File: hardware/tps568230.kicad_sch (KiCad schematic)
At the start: 30 parts, among them U3 TPS568230, U4 LD39050PU33R

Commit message: Annotating components
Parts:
- renumbered TP1 to TP2, TP2 to TP4
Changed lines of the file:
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@@
 		(dnp no)
 		(fields_autoplaced yes)
-		(property "Reference" "#PWR015"
+		(property "Reference" "#PWR016"
 			(at 124.46 87.63 0)
 			(effects
@@
 			(project "chromapi_motherboard_v1"
 				(path "/d1a31f26-03e0-43e1-89c1-031fe31befc5/19a2634a-eca3-4c2c-b35f-9c69362f2888"
-					(reference "#PWR015")
+					(reference "#PWR016")
 					(unit 1)
 				)
@@
 		(dnp no)
 		(fields_autoplaced yes)
-		(property "Reference" "#FLG08"
+		(property "Reference" "#FLG09"
 			(at 187.325 127 0)
 			(effects
@@
 			(project "chromapi_motherboard_v1"
 				(path "/d1a31f26-03e0-43e1-89c1-031fe31befc5/19a2634a-eca3-4c2c-b35f-9c69362f2888"
-					(reference "#FLG08")
+					(reference "#FLG09")
 					(unit 1)
 				)
@@
 		(dnp no)
 		(fields_autoplaced yes)
-		(property "Reference" "#FLG07"
+		(property "Reference" "#FLG08"
 			(at 117.475 127 0)
 			(effects
@@
 			(project "chromapi_motherboard_v1"
 				(path "/d1a31f26-03e0-43e1-89c1-031fe31befc5/19a2634a-eca3-4c2c-b35f-9c69362f2888"
-					(reference "#FLG07")
+					(reference "#FLG08")
 					(unit 1)
 				)
@@
 		(dnp no)
 		(fields_autoplaced yes)
-		(property "Reference" "TP2"
+		(property "Reference" "TP4"
 			(at 236.22 49.0219 0)
 			(effects
@@
 			(project "chromapi_motherboard_v1"
 				(path "/d1a31f26-03e0-43e1-89c1-031fe31befc5/19a2634a-eca3-4c2c-b35f-9c69362f2888"
-					(reference "TP2")
+					(reference "TP4")
 					(unit 1)
 				)
@@
 		(dnp no)
 		(fields_autoplaced yes)
-		(property "Reference" "TP1"
+		(property "Reference" "TP2"
 			(at 82.55 28.4479 0)
 			(effects
@@
 			(project ""
 				(path "/d1a31f26-03e0-43e1-89c1-031fe31befc5/19a2634a-eca3-4c2c-b35f-9c69362f2888"
-					(reference "TP1")
+					(reference "TP2")
 					(unit 1)
 				)
@@
 		(dnp no)
 		(fields_autoplaced yes)
-		(property "Reference" "#PWR016"
+		(property "Reference" "#PWR015"
 			(at 119.38 127 0)
 			(effects
@@
 			(project ""
 				(path "/d1a31f26-03e0-43e1-89c1-031fe31befc5/19a2634a-eca3-4c2c-b35f-9c69362f2888"
-					(reference "#PWR016")
-					(unit 1)
-				)
+					(reference "#PWR015")
+					(unit 1)
+				)

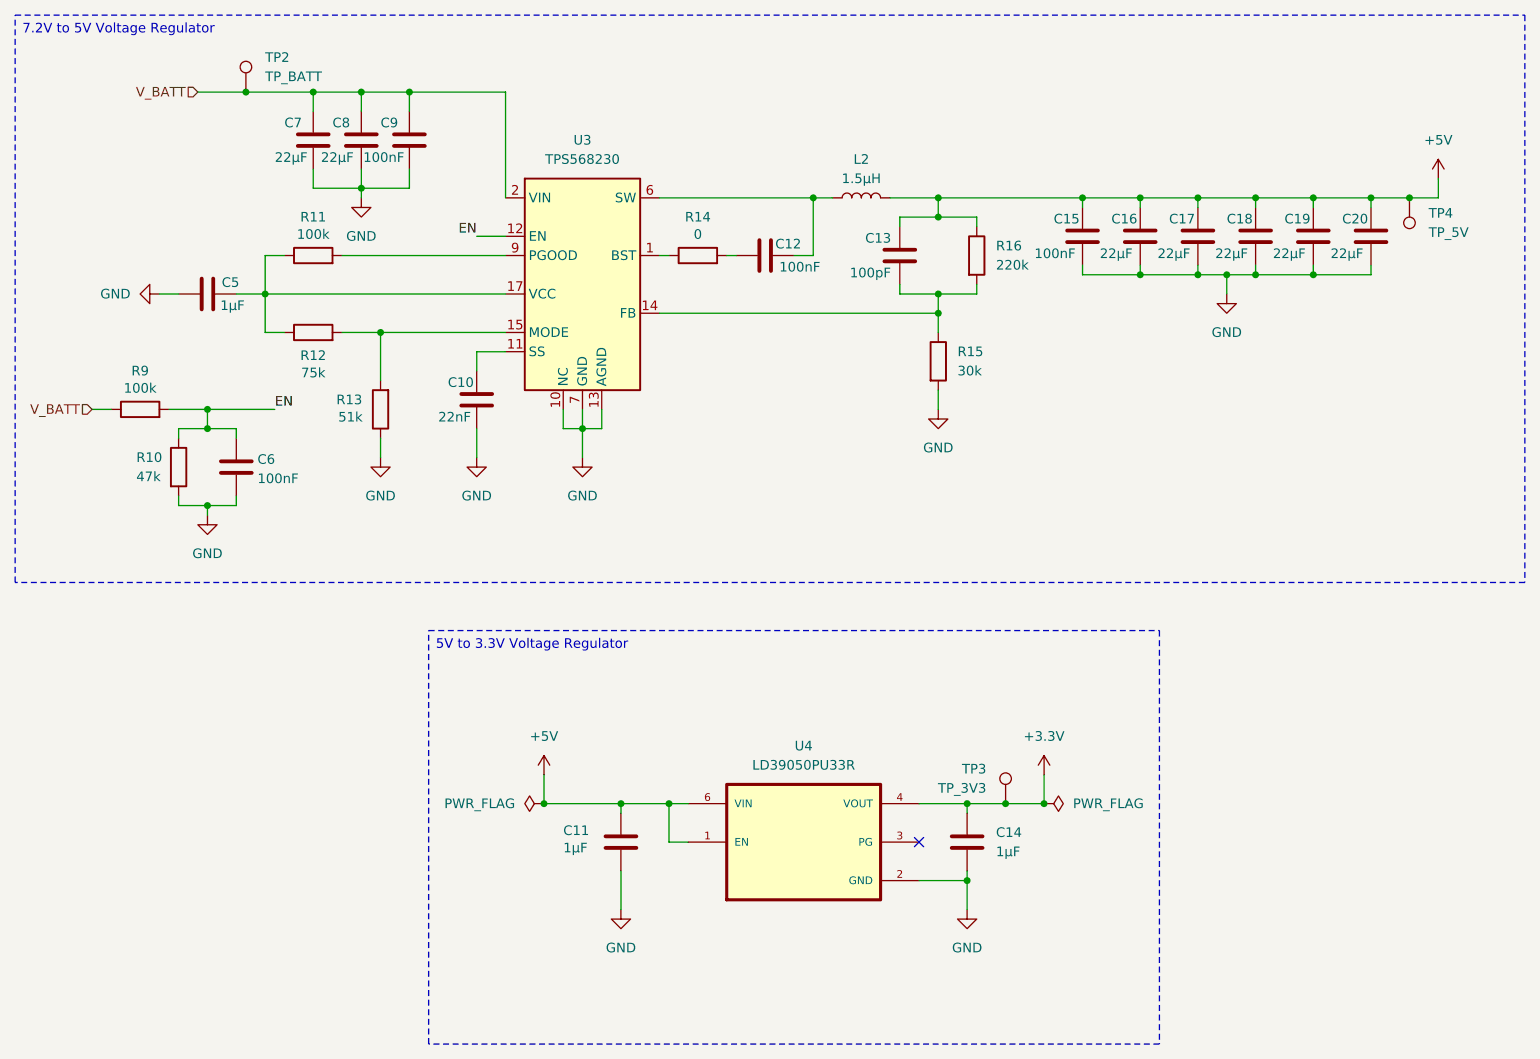
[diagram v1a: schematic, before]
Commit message: Adding power LED status
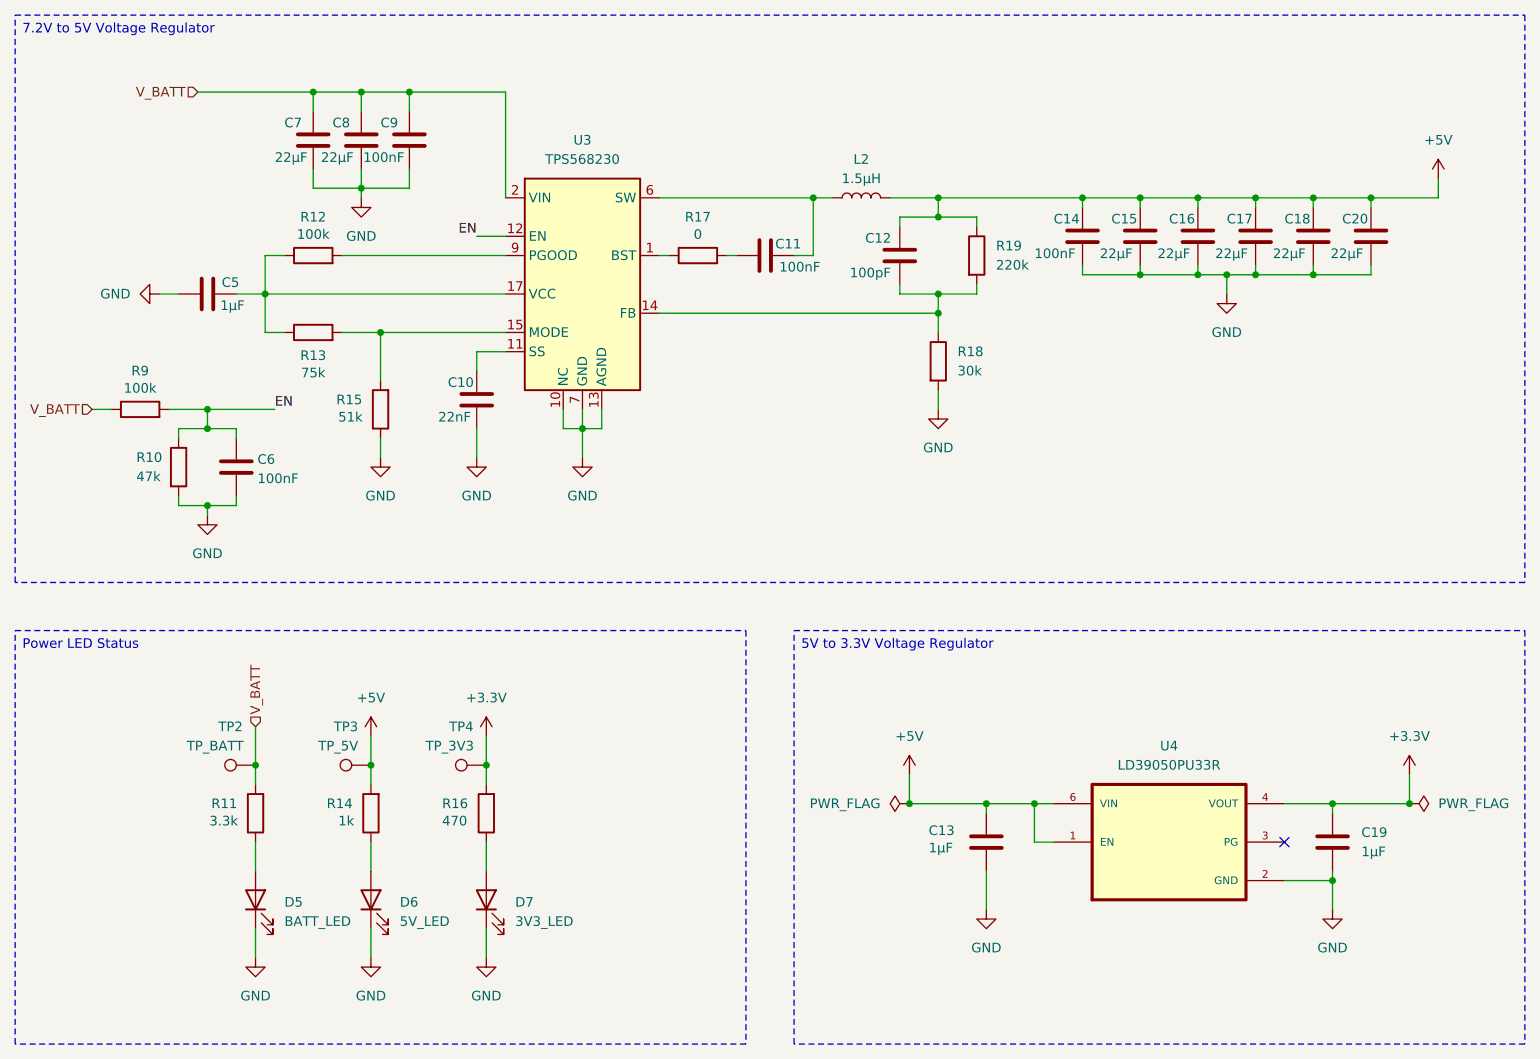
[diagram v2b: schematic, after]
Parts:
- removed TP3: TP_3V3, symbol Connector:TestPoint
- added D5: BATT_LED, symbol Device:LED
- added D6: 5V_LED, symbol Device:LED
- added D7: 3V3_LED, symbol Device:LED
- added R11: 3.3k, symbol Device:R
- added R14: 1k, symbol Device:R
- added R16: 470, symbol Device:R
- added TP4: TP_3V3, symbol Connector:TestPoint
- renumbered C12 to C11, C13 to C12, C11 to C13, C15 to C14, C16 to C15, C17 to C16, C18 to C17, C19 to C18, C14 to C19, R11 to R12, R12 to R13, R13 to R15, R14 to R17, R15 to R18, R16 to R19, TP4 to TP3
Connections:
- net +3.3V: now also R16.2, TP4.1
- net +5V: now also R14.2
- net GND: now also D5.1 (K), D6.1 (K), D7.1 (K)
- net V_BATT: now also R11.2
- new net: D7.2 (A), R16.1
- new net: D5.2 (A), R11.1
- new net: D6.2 (A), R14.1
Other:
- moved on the sheet: C13, C19, TP2, TP3, U4

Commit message: Adding footprint & symbol folders
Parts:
- removed U3: TPS568230, Package_DFN_QFN:Texas_RJE0020A_VQFN-20-1EP_3x3mm_P0.45mm_EP0.675x0.76mm, symbol Regulator_Switching:TPS568230
- removed U4: LD39050PU33R, LD39050PU33R:SON95P300X300X100-7N, symbol LD39050PU33R:LD39050PU33R
- added U3: TPS568230, Package_DFN_QFN:Texas_RJE0020A_VQFN-20-1EP_3x3mm_P0.45mm_EP0.675x0.76mm, symbol tps568230:TPS568230
- added U4: LD39050PU33R, Chromapi_FP:ld39050PU33R_SON95P300X300X100-7N, symbol ld39050pu33r:LD39050PU33R
- renumbered C16 to C10, C17 to C11, C18 to C12, C20 to C13, C11 to C14, C12 to C15, C5 to C16, C10 to C17, C6 to C18, C13 to C19, C19 to C20, C7 to C5, C8 to C6, C9 to C7, C14 to C8, C15 to C9, R17 to R10, R19 to R11, R13 to R12, R18 to R13, R9 to R14, R10 to R16, R11 to R17, R14 to R18, R16 to R19, R12 to R9
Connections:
- net +3.3V: now also U4.4 (VOUT)
- net +5V: now also U4.1 (EN), U4.6 (VIN)
- net EN: now also U3.12 (EN)
- net GND: now also U3.10 (NC), U3.13 (AGND), U3.16 (NC), U3.18 (GND), U3.21 (GND), U3.7 (GND), U3.8 (GND), U4.2 (GND), U4.7 (GND)
- net V_BATT: now also U3.2 (VIN), U3.3 (VIN), U3.4 (VIN), U3.5 (VIN)
- net at C14.1, L2.1: now also U3.19 (SW), U3.20 (SW), U3.6 (SW)
- net at C16.1, R12.1, R9.1: now also U3.17 (VCC)
- net at R12.2, R15.2: now also U3.15 (MODE)
- net at C15.2, R11.2, R13.1: now also U3.14 (FB)
- net at R10.1: now also U3.1 (BST)
- net at C17.1: now also U3.11 (SS)
- net at R9.2: now also U3.9 (PGOOD)

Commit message: Adding cooling fan
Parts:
- D5, D6, D7: footprint (none) -> LED_SMD:LED_0402_1005Metric
- R9: footprint (none) -> LED_SMD:LED_0603_1608Metric
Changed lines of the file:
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@@
 			)
 		)
-		(property "Footprint" ""
+		(property "Footprint" "LED_SMD:LED_0402_1005Metric"
 			(at 111.76 139.7 0)
 			(effects
@@
 			)
 		)
-		(property "Footprint" ""
+		(property "Footprint" "LED_SMD:LED_0603_1608Metric"
 			(at 88.9 56.388 90)
 			(effects
@@
 			)
 		)
-		(property "Footprint" ""
+		(property "Footprint" "LED_SMD:LED_0402_1005Metric"
 			(at 96.52 139.7 0)
 			(effects
@@
 			)
 		)
-		(property "Footprint" ""
+		(property "Footprint" "LED_SMD:LED_0402_1005Metric"
 			(at 81.28 139.7 0)
 			(effects

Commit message: Adding footprints
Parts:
- C19, C20: footprint (none) -> Capacitor_SMD:C_0603_1608Metric
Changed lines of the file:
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@@
 			)
 		)
-		(property "Footprint" ""
+		(property "Footprint" "Capacitor_SMD:C_0603_1608Metric"
 			(at 178.7652 135.89 0)
 			(effects
@@
 					(unit 1)
 				)
+				(path "/d1a31f26-03e0-43e1-89c1-031fe31befc5/2dc5047f-e6b9-4c1e-8ac3-300835122eb4"
+					(reference "U4")
+					(unit 1)
+				)
 			)
 		)
@@
 			)
 		)
-		(property "Footprint" ""
+		(property "Footprint" "Capacitor_SMD:C_0603_1608Metric"
 			(at 224.4852 135.89 0)
 			(effects

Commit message: Updating footprints
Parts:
- C10, C11, C12, C13, C5, C6, C9: footprint (none) -> Capacitor_SMD:C_0805_2012Metric
- C14, C15, C16, C17, C18, C7, C8: footprint (none) -> Capacitor_SMD:C_0603_1608Metric
- L2: footprint (none) -> Inductor_SMD:L_7.3x7.3_H3.5
- R10, R11, R12, R13, R14, R15, R16, R17, R18, R19: footprint (none) -> Resistor_SMD:R_0603_1608Metric
- TP2, TP3, TP4: footprint (none) -> TestPoint:TestPoint_Pad_D1.5mm
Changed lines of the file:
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@@
 			)
 		)
-		(property "Footprint" ""
+		(property "Footprint" "Inductor_SMD:L_7.3x7.3_H3.5"
 			(at 161.29 46.99 0)
 			(effects
@@
 			)
 		)
-		(property "Footprint" ""
+		(property "Footprint" "Capacitor_SMD:C_0603_1608Metric"
 			(at 71.12 60.6552 0)
 			(effects
@@
 			)
 		)
-		(property "Footprint" ""
+		(property "Footprint" "Capacitor_SMD:C_0805_2012Metric"
 			(at 96.2152 43.18 0)
 			(effects
@@
 			)
 		)
-		(property "Footprint" ""
+		(property "Footprint" "Resistor_SMD:R_0603_1608Metric"
 			(at 113.538 128.27 90)
 			(effects
@@
 			)
 		)
-		(property "Footprint" ""
+		(property "Footprint" "Resistor_SMD:R_0603_1608Metric"
 			(at 66.04 76.708 90)
 			(effects
@@
 			)
 		)
-		(property "Footprint" ""
+		(property "Footprint" "Resistor_SMD:R_0603_1608Metric"
 			(at 69.342 82.55 90)
 			(effects
@@
 			)
 		)
-		(property "Footprint" ""
+		(property "Footprint" "Resistor_SMD:R_0603_1608Metric"
 			(at 99.568 74.93 90)
 			(effects
@@
 			)
 		)
-		(property "Footprint" ""
+		(property "Footprint" "Resistor_SMD:R_0603_1608Metric"
 			(at 83.058 128.27 90)
 			(effects
@@
 			)
 		)
-		(property "Footprint" ""
+		(property "Footprint" "Resistor_SMD:R_0603_1608Metric"
 			(at 98.298 128.27 90)
 			(effects
@@
 			)
 		)
-		(property "Footprint" ""
+		(property "Footprint" "Capacitor_SMD:C_0805_2012Metric"
 			(at 199.0852 55.88 0)
 			(effects
@@
 			)
 		)
-		(property "Footprint" ""
+		(property "Footprint" "TestPoint:TestPoint_Pad_D1.5mm"
 			(at 96.52 116.84 0)
 			(effects
@@
 			)
 		)
-		(property "Footprint" ""
+		(property "Footprint" "Resistor_SMD:R_0603_1608Metric"
 			(at 169.672 68.58 90)
 			(effects
@@
 			)
 		)
-		(property "Footprint" ""
+		(property "Footprint" "Resistor_SMD:R_0603_1608Metric"
 			(at 139.7 56.388 90)
 			(effects
@@
 			)
 		)
-		(property "Footprint" ""
+		(property "Footprint" "TestPoint:TestPoint_Pad_D1.5mm"
 			(at 81.28 116.84 0)
 			(effects
@@
 			)
 		)
-		(property "Footprint" ""
+		(property "Footprint" "Capacitor_SMD:C_0805_2012Metric"
 			(at 89.8652 43.18 0)
 			(effects
@@
 			)
 		)
-		(property "Footprint" ""
+		(property "Footprint" "Capacitor_SMD:C_0603_1608Metric"
 			(at 167.3352 58.42 0)
 			(effects
@@
 			)
 		)
-		(property "Footprint" ""
+		(property "Footprint" "TestPoint:TestPoint_Pad_D1.5mm"
 			(at 111.76 116.84 0)
 			(effects
@@
 			)
 		)
-		(property "Footprint" ""
+		(property "Footprint" "Capacitor_SMD:C_0603_1608Metric"
 			(at 79.7052 86.36 0)
 			(effects
@@
 			)
 		)
-		(property "Footprint" ""
+		(property "Footprint" "Resistor_SMD:R_0603_1608Metric"
 			(at 174.752 54.61 90)
 			(effects
@@
 			)
 		)
-		(property "Footprint" ""
+		(property "Footprint" "Resistor_SMD:R_0603_1608Metric"
 			(at 88.9 66.548 90)
 			(effects
@@
 			)
 		)
-		(property "Footprint" ""
+		(property "Footprint" "Capacitor_SMD:C_0805_2012Metric"
 			(at 206.7052 55.88 0)
 			(effects
@@
 			)
 		)
-		(property "Footprint" ""
+		(property "Footprint" "Capacitor_SMD:C_0603_1608Metric"
 			(at 102.5652 43.18 0)
 			(effects
@@
 			)
 		)
-		(property "Footprint" ""
+		(property "Footprint" "Capacitor_SMD:C_0805_2012Metric"
 			(at 221.9452 55.88 0)
 			(effects
@@
 			)
 		)
-		(property "Footprint" ""
+		(property "Footprint" "Capacitor_SMD:C_0603_1608Metric"
 			(at 144.78 55.5752 0)
 			(effects
@@
 			)
 		)
-		(property "Footprint" ""
+		(property "Footprint" "Capacitor_SMD:C_0603_1608Metric"
 			(at 191.4652 55.88 0)
 			(effects
@@
 			)
 		)
-		(property "Footprint" ""
+		(property "Footprint" "Capacitor_SMD:C_0805_2012Metric"
 			(at 229.5652 55.88 0)
 			(effects
@@
 			)
 		)
-		(property "Footprint" ""
+		(property "Footprint" "Capacitor_SMD:C_0603_1608Metric"
 			(at 111.4552 77.47 0)
 			(effects
@@
 			)
 		)
-		(property "Footprint" ""
+		(property "Footprint" "Capacitor_SMD:C_0805_2012Metric"
 			(at 214.3252 55.88 0)
 			(effects

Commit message: Modyfing components footprints
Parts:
- C15, C18: footprint Capacitor_SMD:C_0603_1608Metric -> Capacitor_SMD:C_0402_1005Metric
- R17, R18, R19: footprint Resistor_SMD:R_0603_1608Metric -> Resistor_SMD:R_0402_1005Metric

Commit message: minor fixes
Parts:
- C14: footprint Capacitor_SMD:C_0603_1608Metric -> Capacitor_SMD:C_0402_1005Metric
- R10: footprint Resistor_SMD:R_0603_1608Metric -> Resistor_SMD:R_0402_1005Metric_Pad0.72x0.64mm_HandSolder
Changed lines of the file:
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@@
 			)
 		)
-		(property "Footprint" "Resistor_SMD:R_0603_1608Metric"
+		(property "Footprint" "Resistor_SMD:R_0402_1005Metric_Pad0.72x0.64mm_HandSolder"
 			(at 139.7 56.388 90)
 			(effects
@@
 			)
 		)
-		(property "Footprint" "Capacitor_SMD:C_0603_1608Metric"
+		(property "Footprint" "Capacitor_SMD:C_0402_1005Metric"
 			(at 144.78 55.5752 0)
 			(effects
